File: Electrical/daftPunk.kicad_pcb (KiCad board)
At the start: 2 copper layers, 12.3 x 64.4 mm, 18 parts, among them J1 Conn_01x03_Male, J2 Conn_01x03_Female

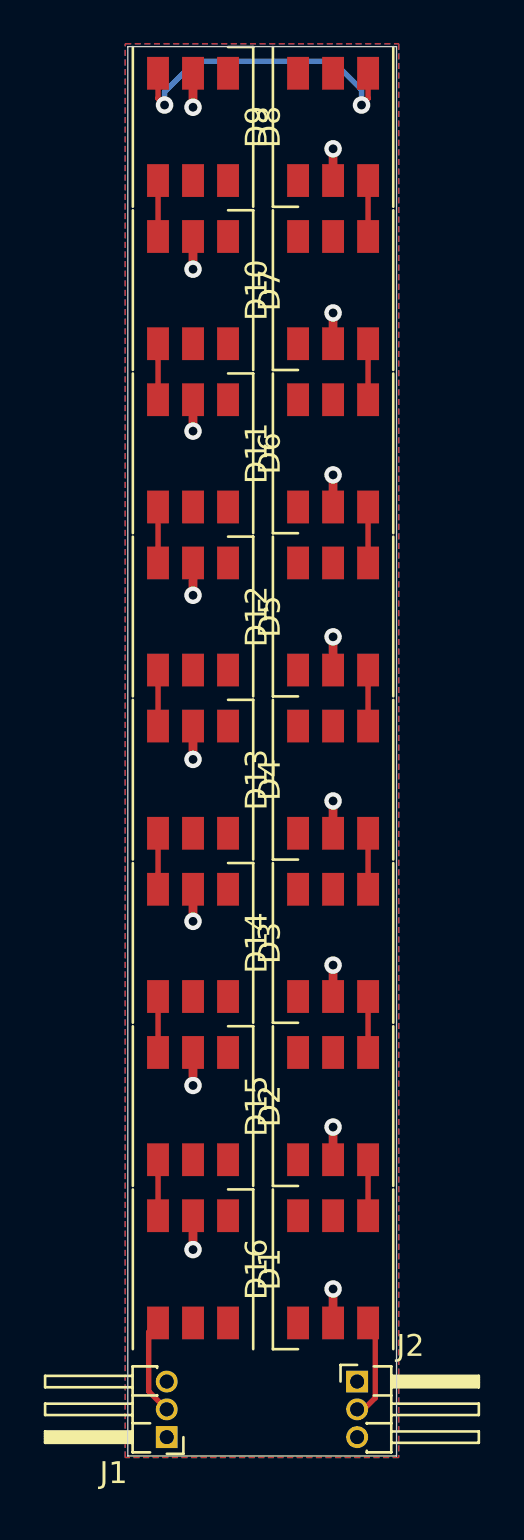
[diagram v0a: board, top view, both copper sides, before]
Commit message: PCB updated to only have pads for board interconnect
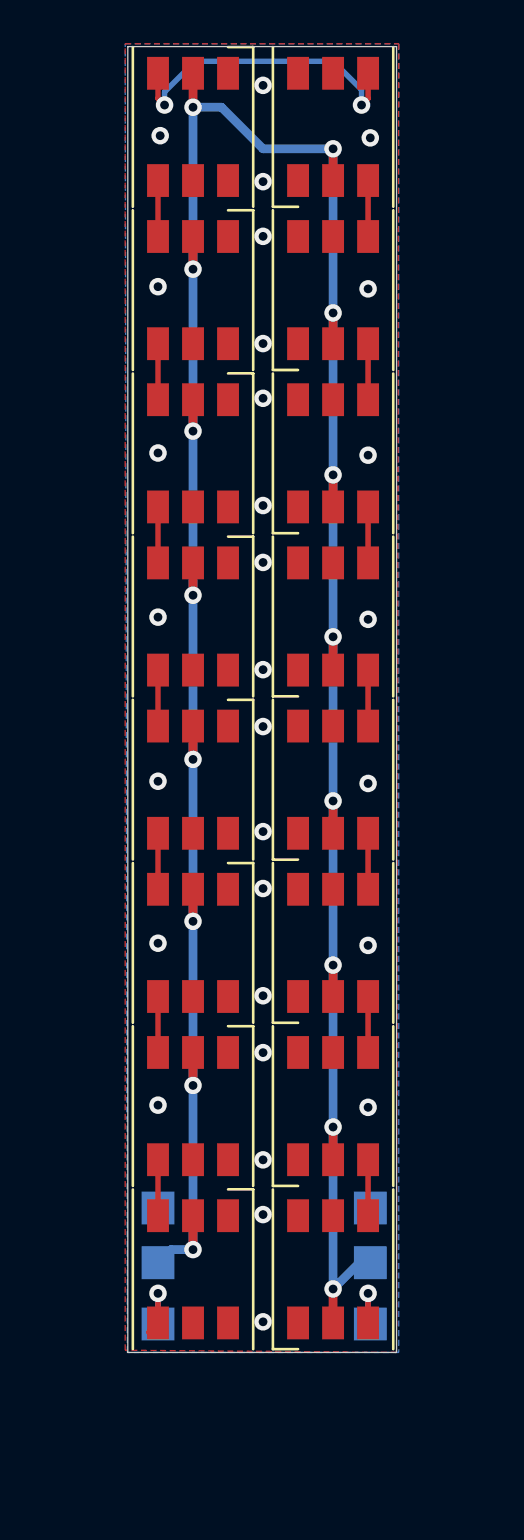
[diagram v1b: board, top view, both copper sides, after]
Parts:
- added J3: Conn_01x01_Female, TestPoint:TestPoint_Pad_1.5x1.5mm, B.Cu at (146.6, 82.7)
- added J4: Conn_01x01_Female, TestPoint:TestPoint_Pad_1.5x1.5mm, B.Cu at (156.3, 85.2)
- added J5: Conn_01x01_Female, TestPoint:TestPoint_Pad_1.5x1.5mm, B.Cu at (156.3, 88.0)
- added J6: Conn_01x01_Female, TestPoint:TestPoint_Pad_1.5x1.5mm, B.Cu at (156.3, 82.7)
- J1: value Conn_01x03_Male -> Conn_01x01_Female; footprint Connector_PinHeader_1.27mm:PinHeader_1x03_P1.27mm_Horizontal -> TestPoint:TestPoint_Pad_1.5x1.5mm; moved to B.Cu
- J2: value Conn_01x03_Female -> Conn_01x01_Female; footprint Connector_PinHeader_1.27mm:PinHeader_1x03_P1.27mm_Horizontal -> TestPoint:TestPoint_Pad_1.5x1.5mm; moved to B.Cu
- moved J2 9.47 mm to (146.6, 88.0)
- moved J1 7.98 mm to (146.6, 85.2), turned to 0 degrees
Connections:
- J1 pad 1: GND -> VDD
- J2 pad 1: VDD -> DIN
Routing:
- net VDD: track 23.8 -> 139.3 mm
- net DOUT: track 4.60 -> 3.35 mm, vias 0 -> 1
- net DIN: track 4.47 -> 3.25 mm, vias 0 -> 1
- net GND: vias 0 -> 30
- added copper zone on B.Cu, net GND
- removed copper zone on B.Cu, net VDD
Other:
- board size 12.3 x 64.4 mm -> 12.3 x 59.7 mm
- board text added: "DIN"
- board text added: "DOUT"
- board text added: "GND"
- board text added: "VDD"

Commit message: Sent pcb for assembly review
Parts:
- added G***: LOGO, Logo:logo2, B.Cu at (151.3, 59.4)
